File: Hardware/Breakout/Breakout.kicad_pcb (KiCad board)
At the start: 2 copper layers, 5 parts, among them U1 TDC7200, U2 BUF6021D

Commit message: Upload of hardware changes as of 6pm 06/07/2023
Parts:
- removed REF**: 21-0058I_MXM, MAX9011EUT:21-0058I_MXM
- removed REF**: 21-0075D_MXM, MAX737AXR805:21-0075D_MXM
- added B2: SSD1306, Library:Adafruit_SSD1306_4Pin, F.Cu at (130.8, 120.0)
- added C1: 0.1uF, 06035C104JAT2A:CAPC1608X90N, F.Cu at (88.3, 105.6)
- added C2: 1uF, UWT1HH010MCL1GB:PCAP_4x5.4-ELECT_NCA-L, F.Cu at (95.2, 107.3)
- added C3: 0.1uF, 06035C104JAT2A:CAPC1608X90N, F.Cu at (88.3, 108.1)
- added C4: 0.1uF, 06035C104JAT2A:CAPC1608X90N, F.Cu at (88.3, 110.7)
- added C5: 0.1uF, 06035C104JAT2A:CAPC1608X90N, F.Cu at (88.3, 113.2)
- added J1: Conn_Coaxial, Library:0731375003_BCN_conn, F.Cu at (122.5, 76.1)
- added U3: BUF602ID, BUF602ID:D0008A_N, F.Cu at (124.5, 90.8)
- added U4: MAX9011EUT+T, MAX9011EUT:21-0058I_MXM, F.Cu at (119.3, 88.8)
- B1: value DIPS1524W66P254L5029H1500Q30N -> NUCLEO-G431KB
- U1: value TDC7200 -> TDC7200PWR
- U2: value BUF6021D -> MAX7375AXR805+T; footprint BUF602ID:D0008A_N -> MAX737AXR805:21-0075D_MXM
- moved B1 36.9 mm to (122.3, 98.4), turned to 180 degrees
- moved U1 28.9 mm to (125.8, 102.7), turned to -90 degrees
- moved U2 14.5 mm to (120.4, 98.1)
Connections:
- B1 pad 1: (no net) -> unconnected-(B1-PA9(D1)-Pad1)
- B1 pad 10: (no net) -> TDCTRIG
- B1 pad 11: (no net) -> unconnected-(B1-PF1(D8)-Pad11)
- B1 pad 12: (no net) -> TDCINTERRUPT
- B1 pad 13: (no net) -> TDC_CS
- B1 pad 14: (no net) -> MOSI
- B1 pad 15: (no net) -> MISO
- B1 pad 16: (no net) -> SPICLK
- B1 pad 17: (no net) -> +3.3V
- B1 pad 18: (no net) -> unconnected-(B1-AREF-Pad18)
- B1 pad 19: (no net) -> unconnected-(B1-PA0(A0)-Pad19)
- B1 pad 2: (no net) -> unconnected-(B1-PA10(D0)-Pad2)
- B1 pad 20: (no net) -> unconnected-(B1-PA1(A1)-Pad20)
- B1 pad 21: (no net) -> unconnected-(B1-PA3(A2)-Pad21)
- B1 pad 22: (no net) -> unconnected-(B1-PA4(A3)-Pad22)
- B1 pad 23: (no net) -> unconnected-(B1-PA5(A4)-Pad23)
- B1 pad 24: (no net) -> unconnected-(B1-PA6(A5)-Pad24)
- B1 pad 25: (no net) -> unconnected-(B1-PA7(A6)-Pad25)
- B1 pad 26: (no net) -> DACPin
- B1 pad 27: (no net) -> +5V
- B1 pad 28: (no net) -> unconnected-(B1-~{RST@2}-Pad28)
- B1 pad 29: (no net) -> GND
- B1 pad 3: (no net) -> unconnected-(B1-~{RST@1}-Pad3)
- B1 pad 30: (no net) -> +9V
- B1 pad 4: (no net) -> GND
- B1 pad 5: (no net) -> unconnected-(B1-PA12(D2)-Pad5)
- B1 pad 6: (no net) -> PULSESIG
- B1 pad 7: (no net) -> SDA
- B1 pad 8: (no net) -> SCL
- B1 pad 9: (no net) -> TDCEN
- U1 pad 1: (no net) -> TDCEN
- U1 pad 10: (no net) -> MOSI
- U1 pad 11: (no net) -> TDC_CS
- U1 pad 12: (no net) -> SPICLK
- U1 pad 13: (no net) -> Net-(U1-VREG)
- U1 pad 14: (no net) -> +3.3V
- U1 pad 2: (no net) -> TDCTRIG
- U1 pad 3: (no net) -> PULSESIG
- U1 pad 4: (no net) -> STOP
- U1 pad 5: (no net) -> REFCLK
- U1 pad 6: (no net) -> unconnected-(U1-NC-Pad6)
- U1 pad 7: (no net) -> GND
- U1 pad 8: (no net) -> TDCINTERRUPT
- U1 pad 9: (no net) -> MISO
- U2 pad 1: (no net) -> +3.3V
- U2 pad 2: (no net) -> REFCLK
- U2 pad 3: (no net) -> GND
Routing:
- net GND: track 0.00 -> 73.9 mm, vias 0 -> 4
- net (no net): track 62.0 -> 0.00 mm
- net +3.3V: track 0.00 -> 60.8 mm, vias 0 -> 2
- net SDA: track 0.00 -> 40.3 mm
- net SCL: track 0.00 -> 34.1 mm
- net SPICLK: track 0.00 -> 19.3 mm
- net MOSI: track 0.00 -> 19.1 mm
- net MISO: track 0.00 -> 19.1 mm
- net STOP: track 0.00 -> 14.6 mm
- net TDC_CS: track 0.00 -> 9.21 mm
- net TDCINTERRUPT: track 0.00 -> 8.66 mm, vias 0 -> 1
- net Net-(J1-In): track 0.00 -> 7.36 mm
- net PULSESIG: track 0.00 -> 6.32 mm
- net REFCLK: track 0.00 -> 5.70 mm
- net DACPin: track 0.00 -> 5.07 mm
- added copper zone on B.Cu, net GND
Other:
- board outline added: 35.7 x 55.5 mm

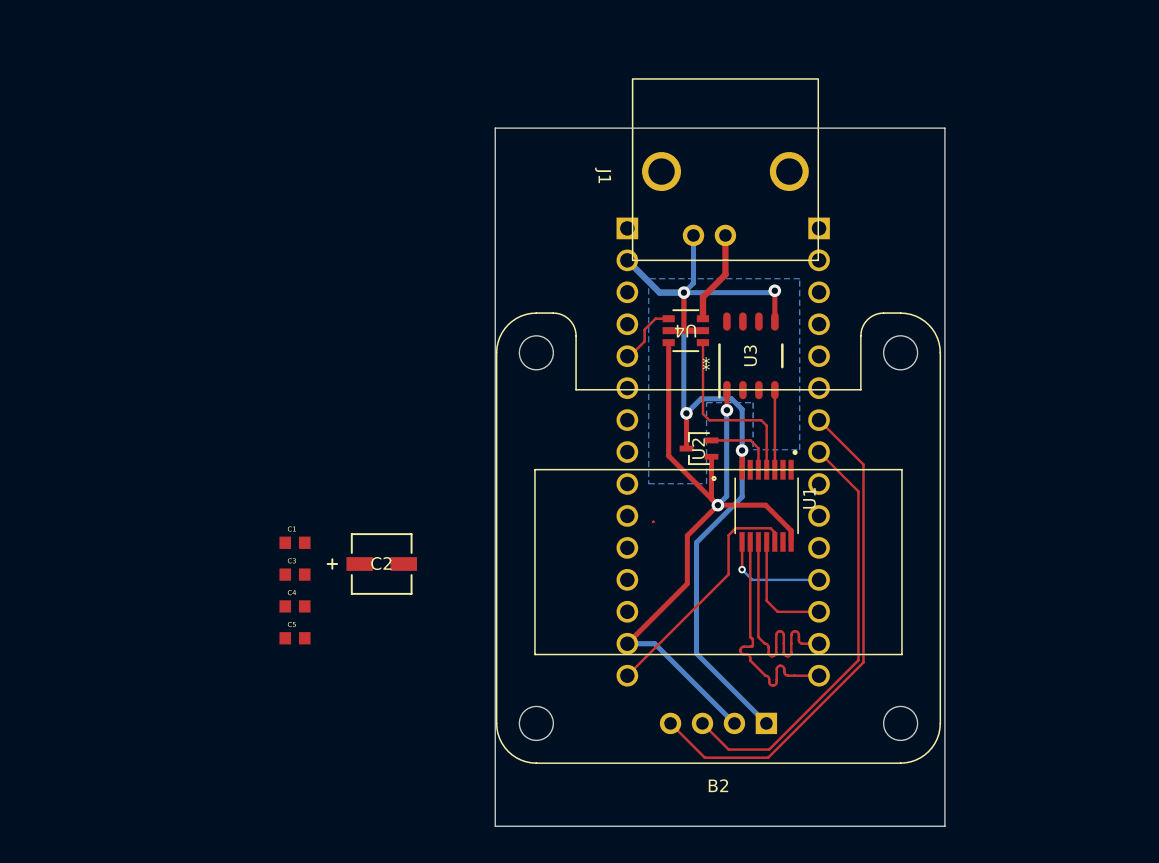
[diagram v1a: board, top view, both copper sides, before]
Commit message: Buttons and fine turning still required
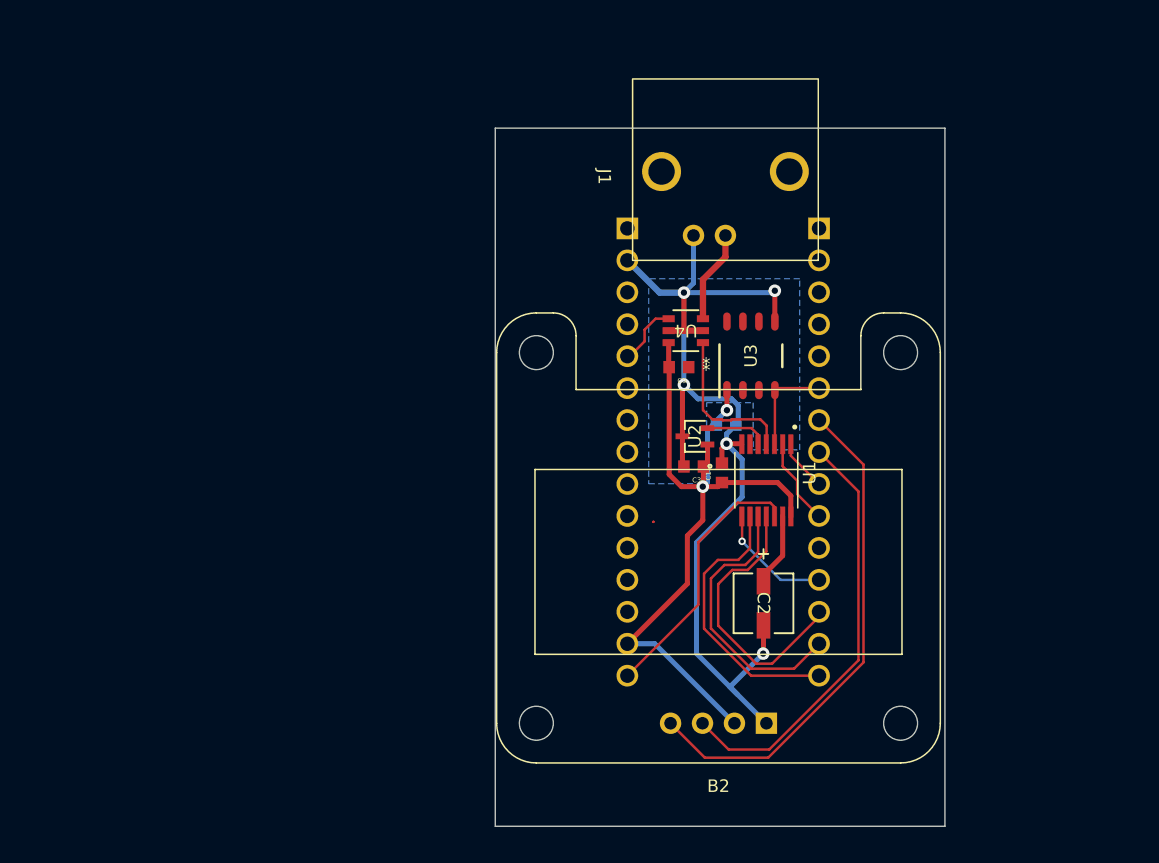
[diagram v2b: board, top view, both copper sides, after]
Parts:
- C4: moved to B.Cu
- moved C5 37.4 mm to (118.8, 91.7), turned to 180 degrees
- moved C4 37.2 mm to (122.5, 96.2), turned to 180 degrees
- moved C1 34.4 mm to (122.2, 100.0), turned to 90 degrees
- moved C3 32.8 mm to (120.0, 99.5), turned to 180 degrees
- moved C2 30.5 mm to (125.5, 110.4), turned to -90 degrees
- moved U1 2.03 mm to (125.8, 100.7)
- moved U2 1.03 mm to (120.1, 97.2)
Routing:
- net TDC_CS: track 9.21 -> 22.2 mm
- net GND: track 73.9 -> 84.9 mm, vias 4 -> 5
- net TDCTRIG: track 0.00 -> 6.90 mm
- net Net-(U1-VREG): track 0.00 -> 5.78 mm
- net TDCEN: track 0.00 -> 4.09 mm
- net MOSI: track 19.1 -> 22.2 mm
- net MISO: track 19.1 -> 22.1 mm
- net STOP: track 14.6 -> 12.5 mm
- net SPICLK: track 19.3 -> 21.2 mm
- net PULSESIG: track 6.32 -> 7.89 mm
- net TDCINTERRUPT: track 8.66 -> 9.37 mm
- net REFCLK: track 5.70 -> 5.01 mm

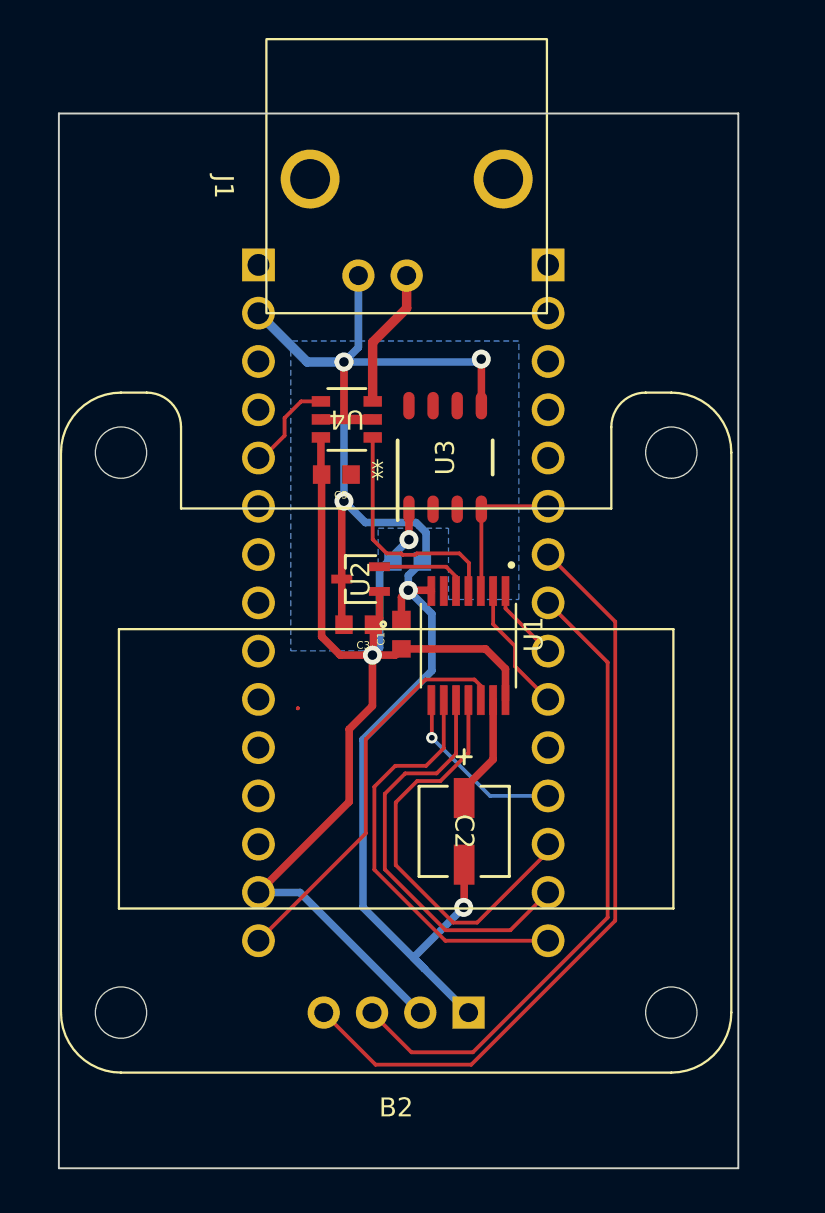
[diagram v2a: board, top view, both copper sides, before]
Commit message: Almost final board, need to fix silkscreen
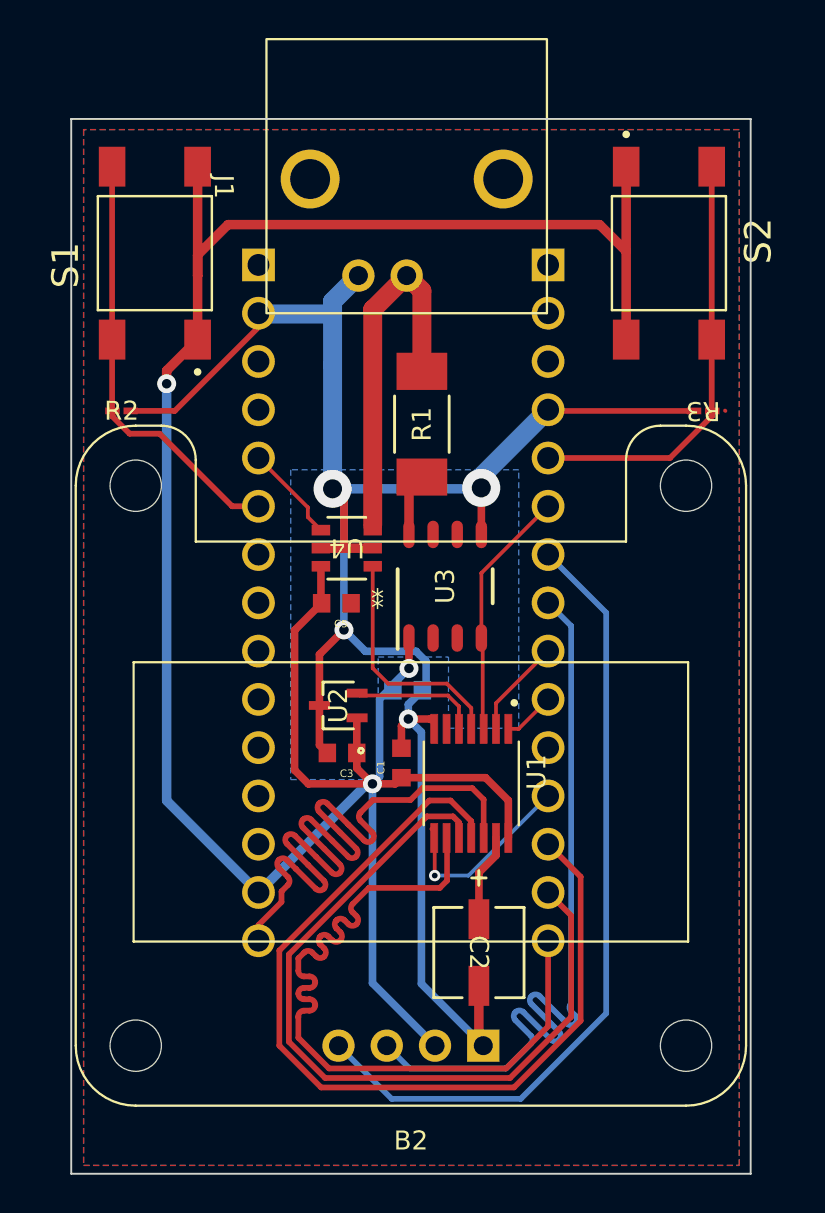
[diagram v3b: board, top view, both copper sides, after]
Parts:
- added R1: 50R, WSC251550R00FEA:RES_WSC_2515-M, F.Cu at (123.3, 89.0)
- added R2: 100k, CRCW0201100KFKED:RC0201N_VIS-M, F.Cu at (107.5, 88.3)
- added R3: 100k, CRCW0201100KFKED:RC0201N_VIS-M, F.Cu at (138.1, 88.3)
- added S1: TL3301PF160QG, TL3301PF160QG:SW_TL3301PF160QG, F.Cu at (109.2, 80.0)
- added S2: TL3301PF160QG, TL3301PF160QG:SW_TL3301PF160QG, F.Cu at (136.3, 80.0)
- moved U1 7.25 mm to (125.9, 107.9)
- moved C3 6.81 mm to (119.1, 106.3)
- moved C1 6.78 mm to (122.2, 106.8)
- moved C4 6.78 mm to (122.5, 103.0)
- moved U3 6.78 mm to (124.5, 97.5)
- moved U4 6.78 mm to (119.3, 95.5)
- moved C5 6.77 mm to (118.8, 98.4)
- moved U2 6.75 mm to (118.9, 103.8)
- moved C2 6.42 mm to (126.3, 116.8)
- moved B2 1.90 mm to (131.6, 121.7)
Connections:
- B1 pad 10: TDCTRIG -> TDCEN
- B1 pad 25: unconnected-(B1-PA7(A6)-Pad25) -> Button 1
- B1 pad 5: unconnected-(B1-PA12(D2)-Pad5) -> Button 2
- B1 pad 9: TDCEN -> TDCTRIG
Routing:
- net +3.3V: track 61.0 -> 137.0 mm, vias 2 -> 3
- net TDC_CS: track 22.2 -> 48.3 mm
- net Button 1: track 0.00 -> 22.8 mm
- net Button 2: track 0.00 -> 22.7 mm
- net SPICLK: track 21.2 -> 41.3 mm
- net MOSI: track 22.2 -> 41.5 mm
- net MISO: track 22.1 -> 41.3 mm
- net GND: track 84.9 -> 103.5 mm, vias 5 -> 4
- net Net-(J1-In): track 7.36 -> 19.2 mm
- net SCL: track 34.1 -> 42.4 mm
- net PULSESIG: track 7.89 -> 13.4 mm
- net Net-(U3-OUT): track 0.00 -> 3.30 mm
- net SDA: track 40.3 -> 42.5 mm
- net REFCLK: track 5.01 -> 6.83 mm
- net TDCTRIG: track 6.90 -> 5.23 mm
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- added copper zone on F.Cu, net GND
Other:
- board size 35.7 x 55.5 mm -> 35.8 x 55.5 mm

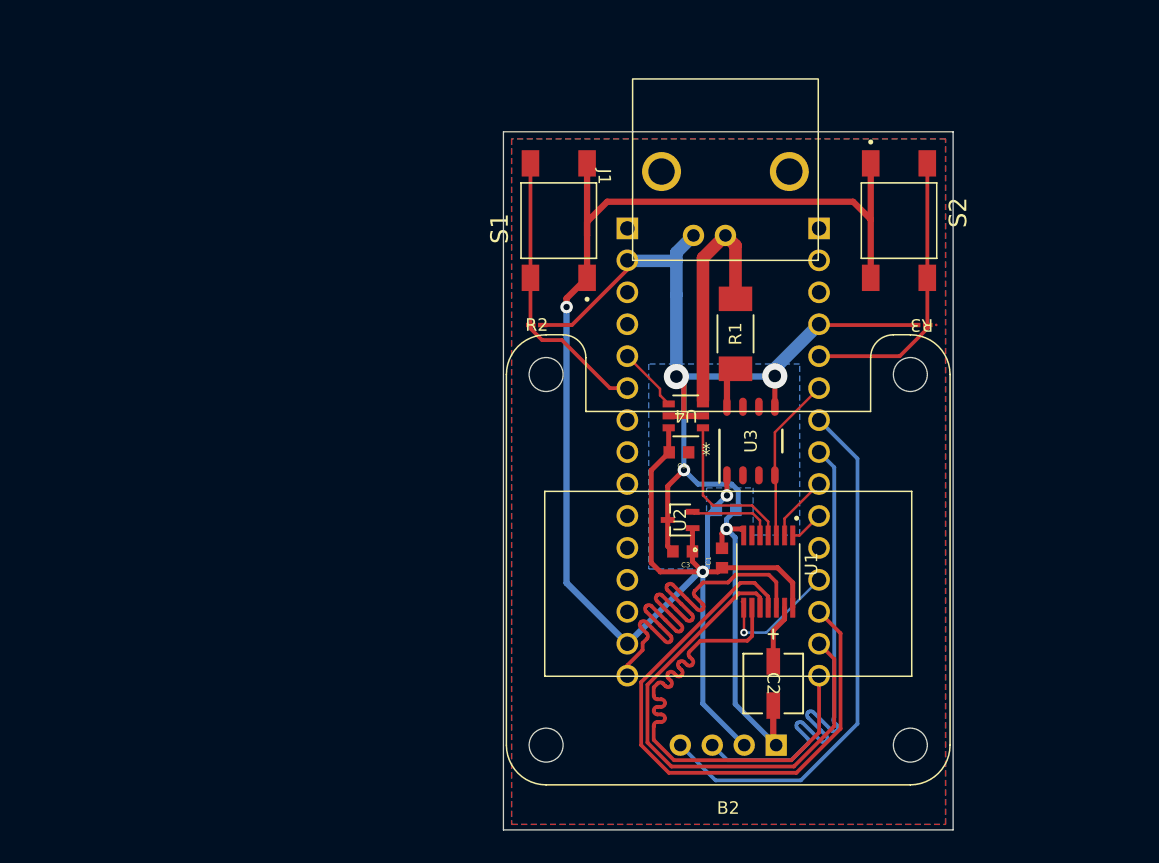
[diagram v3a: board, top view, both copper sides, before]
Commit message: adjusted IC footprints, DRC massaging, added test points, added 9v input pins,
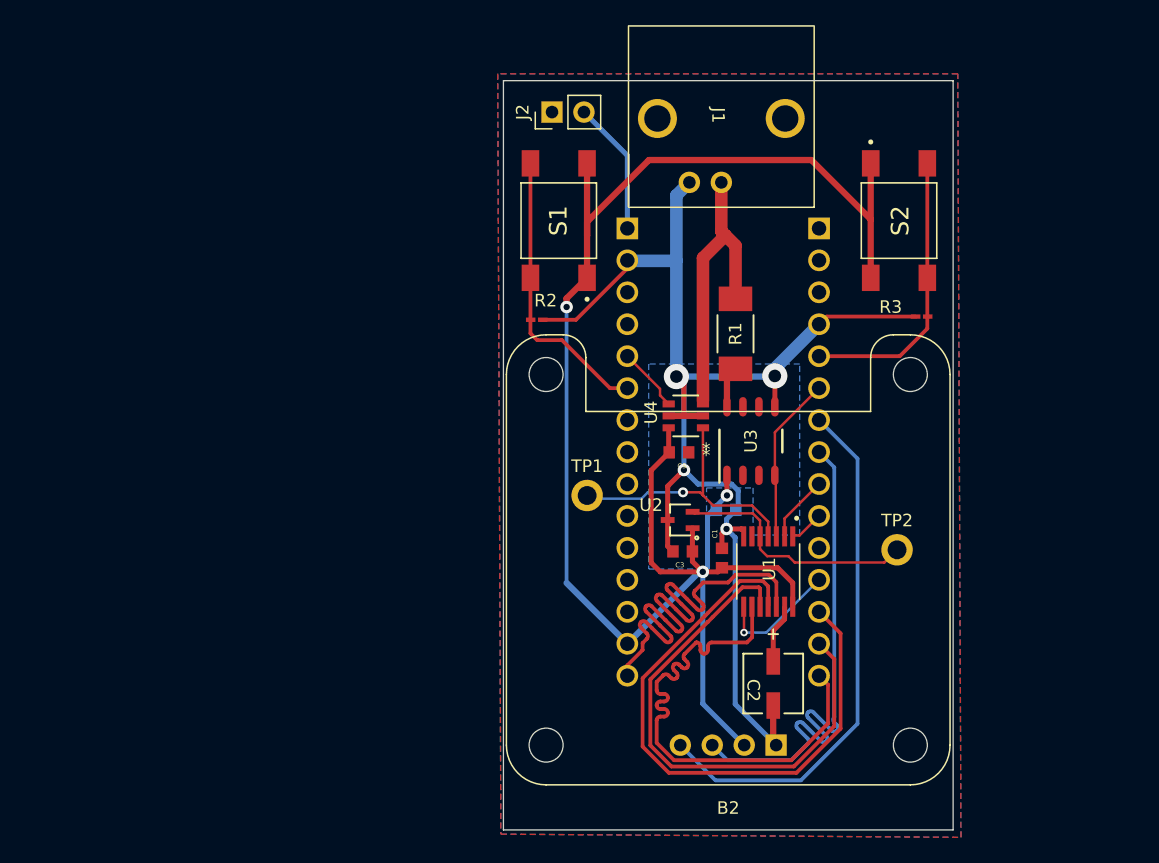
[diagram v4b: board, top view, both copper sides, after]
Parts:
- added J2: 9v_batt_in, Connector_PinHeader_2.54mm:PinHeader_1x02_P2.54mm_Vertical, F.Cu at (108.7, 71.4)
- added TP1: TestPoint, Connector_PinHeader_2.54mm:PinHeader_1x01_P2.54mm_Vertical, F.Cu at (111.5, 101.9)
- added TP2: TestPoint, Connector_PinHeader_2.54mm:PinHeader_1x01_P2.54mm_Vertical, F.Cu at (136.1, 106.2)
- moved J1 4.23 mm to (122.2, 71.9)
- moved R3 0.67 mm to (138.1, 87.6)
- moved R2 0.42 mm to (107.5, 87.9)
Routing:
- net REFCLK: track 6.83 -> 19.6 mm
- net +9V: track 0.00 -> 10.7 mm
- net STOP: track 12.5 -> 22.1 mm, vias 0 -> 1
- net Net-(J1-In): track 19.2 -> 23.6 mm
- net GND: track 103.5 -> 106.9 mm
- net +3.3V: track 137.0 -> 139.0 mm
- net MISO: track 41.3 -> 42.0 mm
- net MOSI: track 41.5 -> 42.2 mm
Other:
- board size 35.8 x 55.5 mm -> 35.8 x 59.6 mm

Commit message: fixed DAC pin
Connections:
- B1 pad 22: unconnected-(B1-PA4(A3)-Pad22) -> DACPin
- B1 pad 26: DACPin -> unconnected-(B1-PA2(A7)-Pad26)
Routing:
- net DACPin: track 5.16 -> 8.52 mm
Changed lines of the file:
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@@
   (net 14 "DACPin")
   (net 15 "unconnected-(B1-PA3(A2)-Pad21)")
-  (net 16 "unconnected-(B1-PA4(A3)-Pad22)")
+  (net 16 "unconnected-(B1-PA2(A7)-Pad26)")
   (net 17 "unconnected-(B1-PA5(A4)-Pad23)")
   (net 18 "unconnected-(B1-PA6(A5)-Pad24)")
@@
       (net 15 "unconnected-(B1-PA3(A2)-Pad21)") (pinfunction "PA3(A2)") (pintype "bidirectional"))
     (pad "22" thru_hole circle (at 7.62 -2.54 180) (size 1.725 1.725) (drill 1.15) (layers "*.Cu" "*.Mask")
-      (net 16 "unconnected-(B1-PA4(A3)-Pad22)") (pinfunction "PA4(A3)") (pintype "bidirectional"))
+      (net 14 "DACPin") (pinfunction "PA4(A3)") (pintype "bidirectional"))
     (pad "23" thru_hole circle (at 7.62 0 180) (size 1.725 1.725) (drill 1.15) (layers "*.Cu" "*.Mask")
       (net 17 "unconnected-(B1-PA5(A4)-Pad23)") (pinfunction "PA5(A4)") (pintype "bidirectional"))
@@
       (net 38 "Button 1") (pinfunction "PA7(A6)") (pintype "bidirectional"))
     (pad "26" thru_hole circle (at 7.62 7.62 180) (size 1.725 1.725) (drill 1.15) (layers "*.Cu" "*.Mask")
-      (net 14 "DACPin") (pinfunction "PA2(A7)") (pintype "bidirectional"))
+      (net 16 "unconnected-(B1-PA2(A7)-Pad26)") (pinfunction "PA2(A7)") (pintype "bidirectional"))
     (pad "27" thru_hole circle (at 7.62 10.16 180) (size 1.725 1.725) (drill 1.15) (layers "*.Cu" "*.Mask")
       (net 19 "+5V") (pinfunction "+5V") (pintype "passive"))
@@
   (segment (start 121.075 103.451472) (end 121.526472 103) (width 0.4) (layer "B.Cu") (net 11))
   (segment (start 114.702 113.6395) (end 120.4165 107.925) (width 0.5) (layer "B.Cu") (net 11))
-  (segment (start 117.987549 94.574999) (end 117.3 93.88745) (width 0.2) (layer "F.Cu") (net 14))
-  (segment (start 117.3 93.3775) (end 114.702 90.7795) (width 0.2) (layer "F.Cu") (net 14))
-  (segment (start 117.3 93.88745) (end 117.3 93.3775) (width 0.2) (layer "F.Cu") (net 14))
+  (segment (start 116.625001 94.574999) (end 117.987549 94.574999) (width 0.25) (layer "F.Cu") (net 14))
+  (segment (start 114.702 100.9395) (end 116.2 99.4415) (width 0.25) (layer "F.Cu") (net 14))
+  (segment (start 116.2 99.4415) (end 116.2 95) (width 0.25) (layer "F.Cu") (net 14))
+  (segment (start 116.2 95) (end 116.625001 94.574999) (width 0.25) (layer "F.Cu") (net 14))
   (segment (start 111.252 71.374) (end 114.702 74.824) (width 0.4) (layer "B.Cu") (net 21))
   (segment (start 114.702 74.824) (end 114.702 80.6195) (width 0.4) (layer "B.Cu") (net 21))
